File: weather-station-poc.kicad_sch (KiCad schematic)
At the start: 8 parts

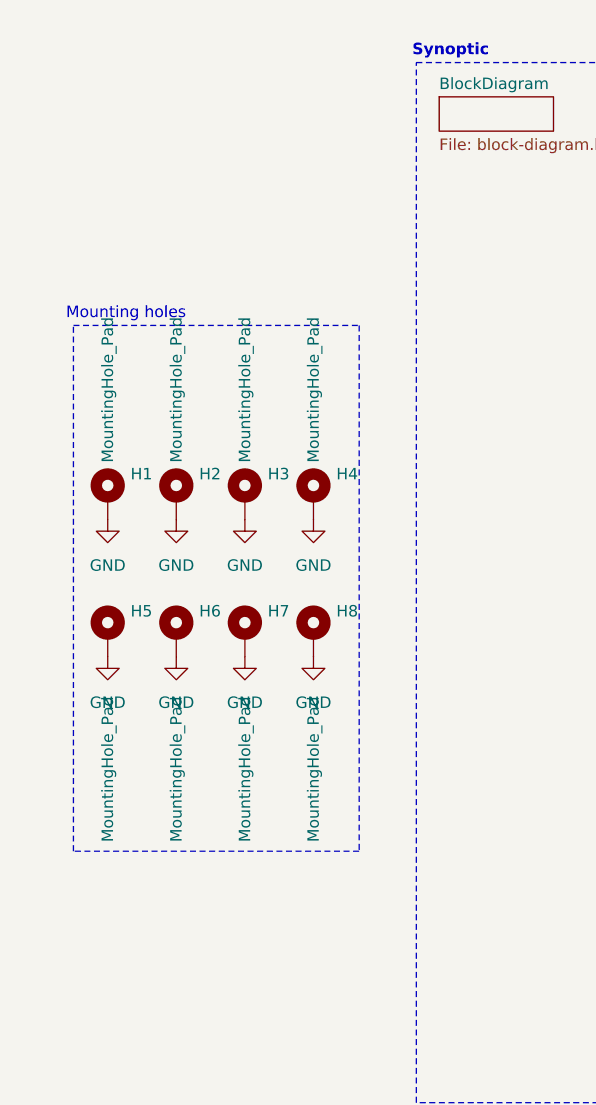
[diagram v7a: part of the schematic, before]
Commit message: Place all vias for GND and add fiducials on top and bottom
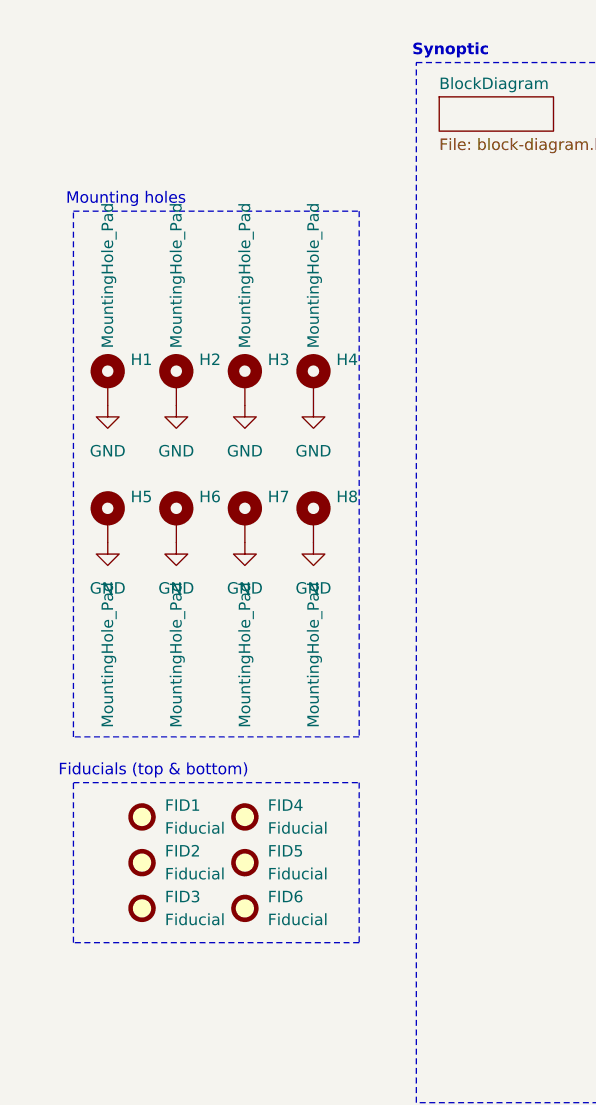
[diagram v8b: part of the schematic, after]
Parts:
- added FID1, FID2, FID3, FID4, FID5, FID6: Fiducial, Fiducial:Fiducial_1mm_Mask2mm, symbol Mechanical:Fiducial
- H1, H2, H3, H4, H5, H6, H7, H8: footprint MountingHole:MountingHole_3.5mm_Pad -> MountingHole:MountingHole_3.5mm_Pad_Via
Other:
- note added: "Fiducials (top & bottom)"
- moved on the sheet: H1, H2, H3, H4, H5, H6, H7, H8
